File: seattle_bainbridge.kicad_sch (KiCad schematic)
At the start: 17 parts

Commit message: single ferry track checkpoint
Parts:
- removed LED458, LED465, LED466, LED467, LED468, LED469: WS2812B-2020, EasyEDA:LED-SMD_4P-L2.0-W2.0-TL_WS2812B-2020, symbol EasyEDA:WS2812B-2020
- added LED430: WS2812B-2020, EasyEDA:LED-SMD_4P-L2.0-W2.0-TL_WS2812B-2020, symbol EasyEDA:WS2812B-2020
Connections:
- net +VLED: now also LED430.4 (VDD); no longer LED425.4 (VDD)
- net GND: now also LED430.2 (GND)
- net at LED464.1 (DO): now also LED424.3 (DI)
- net at LED431.3 (DI): now also LED424.1 (DO); no longer LED429.1 (DO)
- net at LED429.3 (DI): now also LED431.1 (DO); no longer LED428.1 (DO)
- net at LED427.1 (DO): now also LED425.3 (DI); no longer LED428.3 (DI)
- net at LED426.1 (DO): now also LED430.3 (DI); no longer LED427.3 (DI)
- net at LED432.3 (DI): now also LED430.1 (DO); no longer LED431.1 (DO)
- new net: LED427.3 (DI), LED428.1 (DO)
- new net: LED428.3 (DI), LED429.1 (DO)
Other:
- moved on the sheet: LED424, LED463, LED464

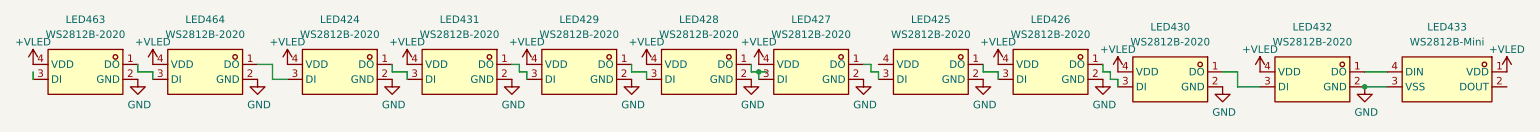
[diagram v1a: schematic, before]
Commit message: Add rail labels
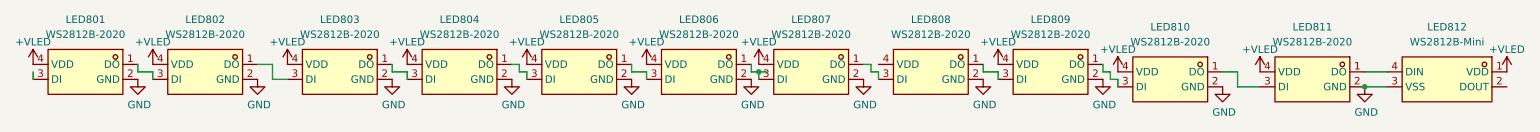
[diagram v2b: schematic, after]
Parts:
- renumbered LED463 to LED801, LED464 to LED802, LED424 to LED803, LED431 to LED804, LED429 to LED805, LED428 to LED806, LED427 to LED807, LED425 to LED808, LED426 to LED809, LED430 to LED810, LED432 to LED811, LED433 to LED812
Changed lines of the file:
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@@
 		(dnp no)
 		(fields_autoplaced yes)
-		(property "Reference" "LED463"
+		(property "Reference" "LED801"
 			(at 38.1 25.4 0)
 			(show_name no)
@@
 			(project "transit"
 				(path "/3763eade-a8c8-4ec0-9cf2-9db4442b4ee5/153adc6e-a3b0-4527-a19a-87e28aab4b4d/86a069a2-ad7e-42b0-b4a6-72695a03f729"
-					(reference "LED463")
+					(reference "LED801")
 					(unit 1)
 				)
@@
 		(in_pos_files yes)
 		(dnp no)
-		(property "Reference" "LED432"
+		(property "Reference" "LED811"
 			(at 246.38 26.67 0)
 			(show_name no)
@@
 			(project "transit"
 				(path "/3763eade-a8c8-4ec0-9cf2-9db4442b4ee5/153adc6e-a3b0-4527-a19a-87e28aab4b4d/86a069a2-ad7e-42b0-b4a6-72695a03f729"
-					(reference "LED432")
+					(reference "LED811")
 					(unit 1)
 				)
@@
 		(in_pos_files yes)
 		(dnp no)
-		(property "Reference" "LED431"
+		(property "Reference" "LED804"
 			(at 101.6 25.4 0)
 			(show_name no)
@@
 			(project "transit"
 				(path "/3763eade-a8c8-4ec0-9cf2-9db4442b4ee5/153adc6e-a3b0-4527-a19a-87e28aab4b4d/86a069a2-ad7e-42b0-b4a6-72695a03f729"
-					(reference "LED431")
+					(reference "LED804")
 					(unit 1)
 				)
@@
 		(dnp no)
 		(fields_autoplaced yes)
-		(property "Reference" "LED430"
+		(property "Reference" "LED810"
 			(at 222.25 26.67 0)
 			(show_name no)
@@
 			(project "transit"
 				(path "/3763eade-a8c8-4ec0-9cf2-9db4442b4ee5/153adc6e-a3b0-4527-a19a-87e28aab4b4d/86a069a2-ad7e-42b0-b4a6-72695a03f729"
-					(reference "LED430")
+					(reference "LED810")
 					(unit 1)
 				)
@@
 		(in_pos_files yes)
 		(dnp no)
-		(property "Reference" "LED433"
+		(property "Reference" "LED812"
 			(at 269.24 26.67 0)
 			(show_name no)
@@
 			(project "transit"
 				(path "/3763eade-a8c8-4ec0-9cf2-9db4442b4ee5/153adc6e-a3b0-4527-a19a-87e28aab4b4d/86a069a2-ad7e-42b0-b4a6-72695a03f729"
-					(reference "LED433")
+					(reference "LED812")
 					(unit 1)
 				)
@@
 		(dnp no)
 		(fields_autoplaced yes)
-		(property "Reference" "LED426"
+		(property "Reference" "LED809"
 			(at 201.93 25.4 0)
 			(show_name no)
@@
 			(project "transit"
 				(path "/3763eade-a8c8-4ec0-9cf2-9db4442b4ee5/153adc6e-a3b0-4527-a19a-87e28aab4b4d/86a069a2-ad7e-42b0-b4a6-72695a03f729"
-					(reference "LED426")
+					(reference "LED809")
 					(unit 1)
 				)
@@
 		(dnp no)
 		(fields_autoplaced yes)
-		(property "Reference" "LED464"
+		(property "Reference" "LED802"
 			(at 58.42 25.4 0)
 			(show_name no)
@@
 			(project "transit"
 				(path "/3763eade-a8c8-4ec0-9cf2-9db4442b4ee5/153adc6e-a3b0-4527-a19a-87e28aab4b4d/86a069a2-ad7e-42b0-b4a6-72695a03f729"
-					(reference "LED464")
+					(reference "LED802")
 					(unit 1)
 				)
@@
 		(dnp no)
 		(fields_autoplaced yes)
-		(property "Reference" "LED425"
+		(property "Reference" "LED808"
 			(at 181.61 25.4 0)
 			(show_name no)
@@
 			(project "transit"
 				(path "/3763eade-a8c8-4ec0-9cf2-9db4442b4ee5/153adc6e-a3b0-4527-a19a-87e28aab4b4d/86a069a2-ad7e-42b0-b4a6-72695a03f729"
-					(reference "LED425")
+					(reference "LED808")
 					(unit 1)
 				)
@@
 		(dnp no)
 		(fields_autoplaced yes)
-		(property "Reference" "LED428"
+		(property "Reference" "LED806"
 			(at 142.24 25.4 0)
 			(show_name no)
@@
 			(project "transit"
 				(path "/3763eade-a8c8-4ec0-9cf2-9db4442b4ee5/153adc6e-a3b0-4527-a19a-87e28aab4b4d/86a069a2-ad7e-42b0-b4a6-72695a03f729"
-					(reference "LED428")
+					(reference "LED806")
 					(unit 1)
 				)
@@
 		(dnp no)
 		(fields_autoplaced yes)
-		(property "Reference" "LED429"
+		(property "Reference" "LED805"
 			(at 121.92 25.4 0)
 			(show_name no)
@@
 			(project "transit"
 				(path "/3763eade-a8c8-4ec0-9cf2-9db4442b4ee5/153adc6e-a3b0-4527-a19a-87e28aab4b4d/86a069a2-ad7e-42b0-b4a6-72695a03f729"
-					(reference "LED429")
+					(reference "LED805")
 					(unit 1)
 				)
@@
 		(dnp no)
 		(fields_autoplaced yes)
-		(property "Reference" "LED427"
+		(property "Reference" "LED807"
 			(at 161.29 25.4 0)
 			(show_name no)
@@
 			(project "transit"
 				(path "/3763eade-a8c8-4ec0-9cf2-9db4442b4ee5/153adc6e-a3b0-4527-a19a-87e28aab4b4d/86a069a2-ad7e-42b0-b4a6-72695a03f729"
-					(reference "LED427")
+					(reference "LED807")
 					(unit 1)
 				)
@@
 		(dnp no)
 		(fields_autoplaced yes)
-		(property "Reference" "LED424"
+		(property "Reference" "LED803"
 			(at 81.28 25.4 0)
 			(show_name no)
@@
 			(project "transit"
 				(path "/3763eade-a8c8-4ec0-9cf2-9db4442b4ee5/153adc6e-a3b0-4527-a19a-87e28aab4b4d/86a069a2-ad7e-42b0-b4a6-72695a03f729"
-					(reference "LED424")
-					(unit 1)
-				)
+					(reference "LED803")
+					(unit 1)
+				)

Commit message: junction checkpoint
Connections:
- net +VLED: now also LED808.4 (VDD)
- net at LED802.3 (DI): now also LED803.1 (DO); no longer LED801.1 (DO)
- net at LED801.3 (DI): now also LED802.1 (DO)
- net at LED811.1 (DO): now also LED810.3 (DI); no longer LED812.4 (DIN)
- net at LED810.1 (DO): now also LED809.3 (DI); no longer LED811.3 (DI)
- net at LED804.1 (DO): now also LED803.3 (DI); no longer LED805.3 (DI)
- net at LED804.3 (DI): now also LED805.1 (DO); no longer LED803.1 (DO)
- net at LED809.1 (DO): now also LED808.3 (DI); no longer LED810.3 (DI)
- net at LED812.2 (DOUT): now also LED811.3 (DI)
- net at LED808.1 (DO): now also LED807.3 (DI); no longer LED809.3 (DI)
- net at LED807.1 (DO): now also LED806.3 (DI); no longer LED808.3 (DI)
- net at LED806.1 (DO): now also LED805.3 (DI); no longer LED807.3 (DI)
- new net BAINBRIDGE_X_KINGSTON: LED801.1 (DO)
- new net BREMERTON_BAINBRIDGE: LED812.4 (DIN)
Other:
- moved on the sheet: LED801, LED810, LED811, LED812

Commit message: reflow reference designators
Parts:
- renumbered LED812 to LED801, LED811 to LED802, LED810 to LED803, LED809 to LED804, LED808 to LED805, LED807 to LED806, LED806 to LED807, LED805 to LED808, LED804 to LED809, LED803 to LED810, LED802 to LED811, LED801 to LED812
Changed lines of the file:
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@@
 		(dnp no)
 		(fields_autoplaced yes)
-		(property "Reference" "LED803"
+		(property "Reference" "LED810"
 			(at 110.49 59.055 0)
 			(show_name no)
@@
 			(project "transit"
 				(path "/3763eade-a8c8-4ec0-9cf2-9db4442b4ee5/153adc6e-a3b0-4527-a19a-87e28aab4b4d/86a069a2-ad7e-42b0-b4a6-72695a03f729"
-					(reference "LED803")
+					(reference "LED810")
 					(unit 1)
 				)
@@
 		(dnp no)
 		(fields_autoplaced yes)
-		(property "Reference" "LED801"
+		(property "Reference" "LED812"
 			(at 160.02 59.055 0)
 			(show_name no)
@@
 			(project "transit"
 				(path "/3763eade-a8c8-4ec0-9cf2-9db4442b4ee5/153adc6e-a3b0-4527-a19a-87e28aab4b4d/86a069a2-ad7e-42b0-b4a6-72695a03f729"
-					(reference "LED801")
+					(reference "LED812")
 					(unit 1)
 				)
@@
 		(dnp no)
 		(fields_autoplaced yes)
-		(property "Reference" "LED809"
+		(property "Reference" "LED804"
 			(at 134.62 28.575 0)
 			(show_name no)
@@
 			(project "transit"
 				(path "/3763eade-a8c8-4ec0-9cf2-9db4442b4ee5/153adc6e-a3b0-4527-a19a-87e28aab4b4d/86a069a2-ad7e-42b0-b4a6-72695a03f729"
-					(reference "LED809")
+					(reference "LED804")
 					(unit 1)
 				)
@@
 		(dnp no)
 		(fields_autoplaced yes)
-		(property "Reference" "LED802"
+		(property "Reference" "LED811"
 			(at 135.255 59.055 0)
 			(show_name no)
@@
 			(project "transit"
 				(path "/3763eade-a8c8-4ec0-9cf2-9db4442b4ee5/153adc6e-a3b0-4527-a19a-87e28aab4b4d/86a069a2-ad7e-42b0-b4a6-72695a03f729"
-					(reference "LED802")
+					(reference "LED811")
 					(unit 1)
 				)
@@
 		(in_pos_files yes)
 		(dnp no)
-		(property "Reference" "LED811"
+		(property "Reference" "LED802"
 			(at 90.805 28.575 0)
 			(show_name no)
@@
 			(project "transit"
 				(path "/3763eade-a8c8-4ec0-9cf2-9db4442b4ee5/153adc6e-a3b0-4527-a19a-87e28aab4b4d/86a069a2-ad7e-42b0-b4a6-72695a03f729"
-					(reference "LED811")
+					(reference "LED802")
 					(unit 1)
 				)
@@
 		(dnp no)
 		(fields_autoplaced yes)
-		(property "Reference" "LED807"
+		(property "Reference" "LED806"
 			(at 177.165 28.575 0)
 			(show_name no)
@@
 			(project "transit"
 				(path "/3763eade-a8c8-4ec0-9cf2-9db4442b4ee5/153adc6e-a3b0-4527-a19a-87e28aab4b4d/86a069a2-ad7e-42b0-b4a6-72695a03f729"
-					(reference "LED807")
+					(reference "LED806")
 					(unit 1)
 				)
@@
 		(dnp no)
 		(fields_autoplaced yes)
-		(property "Reference" "LED805"
+		(property "Reference" "LED808"
 			(at 222.25 29.21 0)
 			(show_name no)
@@
 			(project "transit"
 				(path "/3763eade-a8c8-4ec0-9cf2-9db4442b4ee5/153adc6e-a3b0-4527-a19a-87e28aab4b4d/86a069a2-ad7e-42b0-b4a6-72695a03f729"
-					(reference "LED805")
+					(reference "LED808")
 					(unit 1)
 				)
@@
 		(dnp no)
 		(fields_autoplaced yes)
-		(property "Reference" "LED810"
+		(property "Reference" "LED803"
 			(at 112.395 28.575 0)
 			(show_name no)
@@
 			(project "transit"
 				(path "/3763eade-a8c8-4ec0-9cf2-9db4442b4ee5/153adc6e-a3b0-4527-a19a-87e28aab4b4d/86a069a2-ad7e-42b0-b4a6-72695a03f729"
-					(reference "LED810")
+					(reference "LED803")
 					(unit 1)
 				)
@@
 		(dnp no)
 		(fields_autoplaced yes)
-		(property "Reference" "LED808"
+		(property "Reference" "LED805"
 			(at 154.94 28.575 0)
 			(show_name no)
@@
 			(project "transit"
 				(path "/3763eade-a8c8-4ec0-9cf2-9db4442b4ee5/153adc6e-a3b0-4527-a19a-87e28aab4b4d/86a069a2-ad7e-42b0-b4a6-72695a03f729"
-					(reference "LED808")
+					(reference "LED805")
 					(unit 1)
 				)
@@
 		(in_pos_files yes)
 		(dnp no)
-		(property "Reference" "LED812"
+		(property "Reference" "LED801"
 			(at 68.58 28.575 0)
 			(show_name no)
@@
 			(project "transit"
 				(path "/3763eade-a8c8-4ec0-9cf2-9db4442b4ee5/153adc6e-a3b0-4527-a19a-87e28aab4b4d/86a069a2-ad7e-42b0-b4a6-72695a03f729"
-					(reference "LED812")
+					(reference "LED801")
 					(unit 1)
 				)
@@
 		(in_pos_files yes)
 		(dnp no)
-		(property "Reference" "LED804"
+		(property "Reference" "LED809"
 			(at 85.725 58.42 0)
 			(show_name no)
@@
 			(project "transit"
 				(path "/3763eade-a8c8-4ec0-9cf2-9db4442b4ee5/153adc6e-a3b0-4527-a19a-87e28aab4b4d/86a069a2-ad7e-42b0-b4a6-72695a03f729"
-					(reference "LED804")
+					(reference "LED809")
 					(unit 1)
 				)
@@
 		(dnp no)
 		(fields_autoplaced yes)
-		(property "Reference" "LED806"
+		(property "Reference" "LED807"
 			(at 199.39 28.575 0)
 			(show_name no)
@@
 			(project "transit"
 				(path "/3763eade-a8c8-4ec0-9cf2-9db4442b4ee5/153adc6e-a3b0-4527-a19a-87e28aab4b4d/86a069a2-ad7e-42b0-b4a6-72695a03f729"
-					(reference "LED806")
-					(unit 1)
-				)
+					(reference "LED807")
+					(unit 1)
+				)

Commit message: rev-b validation run
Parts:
- LED802, LED803, LED804, LED805, LED806, LED807, LED808, LED809, LED810, LED811, LED812: LCSC Part C965555 -> C52917434
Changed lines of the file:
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@@
 	(paper "A4")
 	(junction
-		(at 99.695 38.735)
-		(diameter 0)
-		(color 0 0 0 0)
-	)
-	(junction
-		(at 99.695 36.195)
-		(diameter 0)
-		(color 0 0 0 0)
-	)
-	(junction
 		(at 78.74 36.195)
 		(diameter 0)
@@
 	(wire
 		(pts
-			(xy 99.695 38.735) (xy 95.885 38.735)
-		)
-		(stroke
-			(width 0)
-			(type default)
-		)
-	)
-	(wire
-		(pts
 			(xy 146.05 37.465) (xy 146.05 38.735)
 		)
@@
 		)
 	)
-	(wire
-		(pts
-			(xy 95.885 36.195) (xy 99.695 36.195)
-		)
-		(stroke
-			(width 0)
-			(type default)
-		)
-	)
 	(global_label "BAINBRIDGE_X_KINGSTON"
 		(shape input)
@@
 			)
 		)
-		(property "Datasheet" "https://lcsc.com/product-detail/Light-Emitting-Diodes-LED_Worldsemi-WS2812B-2020_C965555.html"
+		(property "Datasheet" "https://lcsc.com/product-detail/Light-Emitting-Diodes-LED_Worldsemi-WS2812B-2020_C52917434.html"
 			(at 119.38 79.375 0)
 			(hide yes)
@@
 			)
 		)
-		(property "LCSC Part" "C965555"
+		(property "LCSC Part" "C52917434"
 			(at 119.38 81.915 0)
 			(hide yes)
@@
 			)
 		)
-		(property "Datasheet" "https://lcsc.com/product-detail/Light-Emitting-Diodes-LED_Worldsemi-WS2812B-2020_C965555.html"
+		(property "Datasheet" "https://lcsc.com/product-detail/Light-Emitting-Diodes-LED_Worldsemi-WS2812B-2020_C52917434.html"
 			(at 168.91 79.375 0)
 			(hide yes)
@@
 			)
 		)
-		(property "LCSC Part" "C965555"
+		(property "LCSC Part" "C52917434"
 			(at 168.91 81.915 0)
 			(hide yes)
@@
 			)
 		)
-		(property "Datasheet" "https://lcsc.com/product-detail/Light-Emitting-Diodes-LED_Worldsemi-WS2812B-2020_C965555.html"
+		(property "Datasheet" "https://lcsc.com/product-detail/Light-Emitting-Diodes-LED_Worldsemi-WS2812B-2020_C52917434.html"
 			(at 143.51 48.895 0)
 			(hide yes)
@@
 			)
 		)
-		(property "LCSC Part" "C965555"
+		(property "LCSC Part" "C52917434"
 			(at 143.51 51.435 0)
 			(hide yes)
@@
 			)
 		)
-		(property "Datasheet" "https://lcsc.com/product-detail/Light-Emitting-Diodes-LED_Worldsemi-WS2812B-2020_C965555.html"
+		(property "Datasheet" "https://lcsc.com/product-detail/Light-Emitting-Diodes-LED_Worldsemi-WS2812B-2020_C52917434.html"
 			(at 144.145 79.375 0)
 			(hide yes)
@@
 			)
 		)
-		(property "LCSC Part" "C965555"
+		(property "LCSC Part" "C52917434"
 			(at 144.145 81.915 0)
 			(hide yes)
@@
 			)
 		)
-		(property "Datasheet" "https://lcsc.com/product-detail/Light-Emitting-Diodes-LED_Worldsemi-WS2812B-2020_C965555.html"
+		(property "Datasheet" "https://lcsc.com/product-detail/Light-Emitting-Diodes-LED_Worldsemi-WS2812B-2020_C52917434.html"
 			(at 99.695 48.895 0)
 			(hide yes)
@@
 			)
 		)
-		(property "LCSC Part" "C965555"
+		(property "LCSC Part" "C52917434"
 			(at 99.695 51.435 0)
 			(hide yes)
@@
 			)
 		)
-		(property "Datasheet" "https://lcsc.com/product-detail/Light-Emitting-Diodes-LED_Worldsemi-WS2812B-2020_C965555.html"
+		(property "Datasheet" "https://lcsc.com/product-detail/Light-Emitting-Diodes-LED_Worldsemi-WS2812B-2020_C52917434.html"
 			(at 186.055 48.895 0)
 			(hide yes)
@@
 			)
 		)
-		(property "LCSC Part" "C965555"
+		(property "LCSC Part" "C52917434"
 			(at 186.055 51.435 0)
 			(hide yes)
@@
 			)
 		)
-		(property "Datasheet" "https://lcsc.com/product-detail/Light-Emitting-Diodes-LED_Worldsemi-WS2812B-2020_C965555.html"
+		(property "Datasheet" "https://lcsc.com/product-detail/Light-Emitting-Diodes-LED_Worldsemi-WS2812B-2020_C52917434.html"
 			(at 231.14 49.53 0)
 			(hide yes)
@@
 			)
 		)
-		(property "LCSC Part" "C965555"
+		(property "LCSC Part" "C52917434"
 			(at 231.14 52.07 0)
 			(hide yes)
@@
 			)
 		)
-		(property "Datasheet" "https://lcsc.com/product-detail/Light-Emitting-Diodes-LED_Worldsemi-WS2812B-2020_C965555.html"
+		(property "Datasheet" "https://lcsc.com/product-detail/Light-Emitting-Diodes-LED_Worldsemi-WS2812B-2020_C52917434.html"
 			(at 121.285 48.895 0)
 			(hide yes)
@@
 			)
 		)
-		(property "LCSC Part" "C965555"
+		(property "LCSC Part" "C52917434"
 			(at 121.285 51.435 0)
 			(hide yes)
@@
 			)
 		)
-		(property "Datasheet" "https://lcsc.com/product-detail/Light-Emitting-Diodes-LED_Worldsemi-WS2812B-2020_C965555.html"
+		(property "Datasheet" "https://lcsc.com/product-detail/Light-Emitting-Diodes-LED_Worldsemi-WS2812B-2020_C52917434.html"
 			(at 163.83 48.895 0)
 			(hide yes)
@@
 			)
 		)
-		(property "LCSC Part" "C965555"
+		(property "LCSC Part" "C52917434"
 			(at 163.83 51.435 0)
 			(hide yes)
@@
 			)
 		)
-		(property "Datasheet" "https://lcsc.com/product-detail/Light-Emitting-Diodes-LED_Worldsemi-WS2812B-2020_C965555.html"
+		(property "Datasheet" "https://lcsc.com/product-detail/Light-Emitting-Diodes-LED_Worldsemi-WS2812B-2020_C52917434.html"
 			(at 94.615 78.74 0)
 			(hide yes)
@@
 			)
 		)
-		(property "LCSC Part" "C965555"
+		(property "LCSC Part" "C52917434"
 			(at 94.615 81.28 0)
 			(hide yes)
@@
 			)
 		)
-		(property "Datasheet" "https://lcsc.com/product-detail/Light-Emitting-Diodes-LED_Worldsemi-WS2812B-2020_C965555.html"
+		(property "Datasheet" "https://lcsc.com/product-detail/Light-Emitting-Diodes-LED_Worldsemi-WS2812B-2020_C52917434.html"
 			(at 208.28 48.895 0)
 			(hide yes)
@@
 			)
 		)
-		(property "LCSC Part" "C965555"
+		(property "LCSC Part" "C52917434"
 			(at 208.28 51.435 0)
 			(hide yes)
